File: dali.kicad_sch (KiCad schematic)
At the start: 15 parts, among them J2 DALI BUS, J3 DALI BUS, J4 DALI BUS, Q2 MMBT2222A, U1 TCLT1000, U2 TCLT1000

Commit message: Fix ESP32-S3-DEVKITC-1 bottom right pins
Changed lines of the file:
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@@
 	)
 	(symbol
+		(lib_name "FODM217D_1")
 		(lib_id "Isolator:FODM217D")
 		(at 166.37 29.21 0)

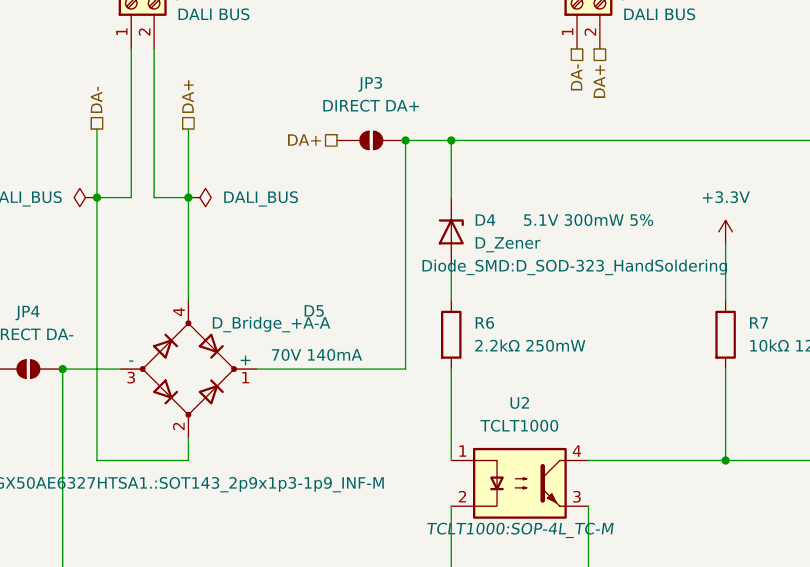
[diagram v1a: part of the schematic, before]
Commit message: Check and list components
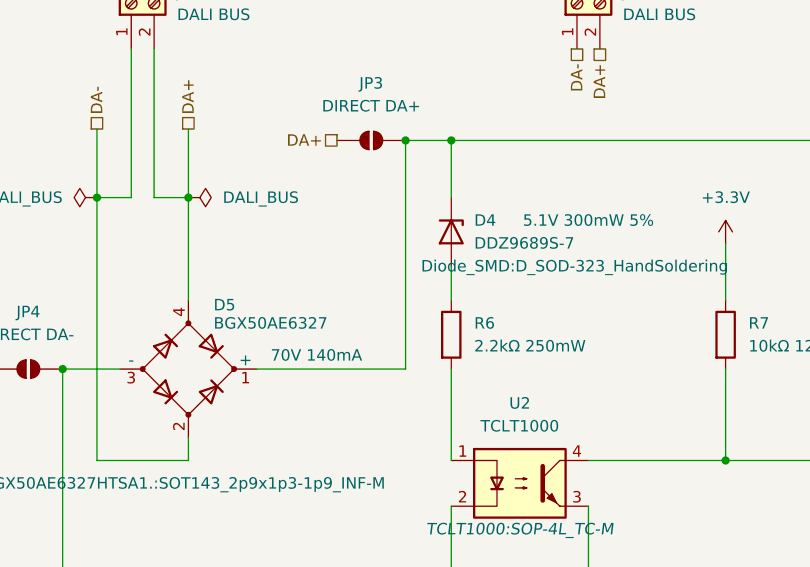
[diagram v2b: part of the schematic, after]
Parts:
- D4: value D_Zener -> DDZ9689S-7
- D5: value D_Bridge_+A-A -> BGX50AE6327
- Q2: footprint Package_TO_SOT_SMD:SOT-23 -> Package_TO_SOT_SMD:SOT-23_Handsoldering
- R6: footprint Resistor_SMD:R_0805_2012Metric_Pad1.20x1.40mm_HandSolder -> Resistor_SMD:R_1206_3216Metric_Pad1.30x1.75mm_HandSolder
- R8: footprint Resistor_SMD:R_0805_2012Metric_Pad1.20x1.40mm_HandSolder -> Resistor_SMD:R_2512_6332Metric_Pad1.40x3.35mm_HandSolder
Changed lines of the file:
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@@
 			)
 		)
-		(property "Footprint" "Resistor_SMD:R_0805_2012Metric_Pad1.20x1.40mm_HandSolder"
+		(property "Footprint" "Resistor_SMD:R_2512_6332Metric_Pad1.40x3.35mm_HandSolder"
 			(at 156.972 49.53 90)
 			(effects
@@
 		(dnp no)
 		(property "Reference" "D5"
-			(at 43.18 45.6498 0)
-			(effects
-				(font
-					(size 1.27 1.27)
-				)
-			)
-		)
-		(property "Value" "D_Bridge_+A-A"
-			(at 31.75 46.99 0)
+			(at 32.004 44.958 0)
+			(effects
+				(font
+					(size 1.27 1.27)
+				)
+				(justify left)
+			)
+		)
+		(property "Value" "BGX50AE6327"
+			(at 32.004 46.99 0)
 			(effects
 				(font
@@
 			)
 		)
-		(property "Datasheet" "~"
+		(property "Datasheet" "https://www.infineon.com/dgdl/bgx50aseries.pdf?folderId=db3a30431400ef6801141cc1c4cd04e8&fileId=db3a30431400ef6801141cc423c404e9"
 			(at 29.21 52.07 0)
 			(effects
@@
 			)
 		)
-		(property "Footprint" "Resistor_SMD:R_0805_2012Metric_Pad1.20x1.40mm_HandSolder"
+		(property "Footprint" "Resistor_SMD:R_1206_3216Metric_Pad1.30x1.75mm_HandSolder"
 			(at 56.642 48.26 90)
 			(effects
@@
 			)
 		)
-		(property "Footprint" "Package_TO_SOT_SMD:SOT-23"
+		(property "Footprint" "Package_TO_SOT_SMD:SOT-23_Handsoldering"
 			(at 118.11 43.815 0)
 			(effects
@@
 			)
 		)
-		(property "Datasheet" "https://assets.nexperia.com/documents/data-sheet/MMBT2222A.pdf"
+		(property "Datasheet" "https://www.onsemi.com/pdf/datasheet/mmbt2222lt1-d.pdf"
 			(at 123.19 41.91 0)
 			(effects
@@
 			)
 		)
-		(property "Value" "D_Zener"
+		(property "Value" "DDZ9689S-7"
 			(at 60.96 38.0999 90)
 			(effects
@@
 			)
 		)
-		(property "Datasheet" "~"
+		(property "Datasheet" "https://www.diodes.com/assets/Datasheets/ds30409.pdf"
 			(at 58.42 36.83 0)
 			(effects

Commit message: Remove the kitchen sink
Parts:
- removed J4: DALI BUS, TerminalBlock:TerminalBlock_bornier-2_P5.08mm, symbol Connector:Screw_Terminal_01x02
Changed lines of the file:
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@@
-		)
-	)
-	(hierarchical_label "DA-"
-		(shape passive)
-		(at 106.68 16.51 270)
-		(effects
-			(font
-				(size 1.27 1.27)
-			)
-			(justify right)
 		)
 	)
@@
 	(hierarchical_label "DA+"
 		(shape passive)
-		(at 109.22 16.51 270)
-		(effects
-			(font
-				(size 1.27 1.27)
-			)
-			(justify right)
-		)
-	)
-	(hierarchical_label "DA+"
-		(shape passive)
 		(at 29.21 25.4 90)
 		(effects
@@
 					(unit 1)
 				)
-			)
-		)
-	)
-	(symbol
-		(lib_id "Connector:Screw_Terminal_01x02")
-		(at 106.68 11.43 90)
-		(unit 1)
-		(exclude_from_sim no)
-		(in_bom yes)
-		(on_board yes)
-		(dnp no)
-		(fields_autoplaced yes)
-		(property "Reference" "J4"
-			(at 111.76 10.1599 90)
-			(effects
-				(font
-					(size 1.27 1.27)
-				)
-				(justify right)
-			)
-		)
-		(property "Value" "DALI BUS"
-			(at 111.76 12.6999 90)
-			(effects
-				(font
-					(size 1.27 1.27)
-				)
-				(justify right)
-			)
-		)
-		(property "Footprint" "TerminalBlock:TerminalBlock_bornier-2_P5.08mm"
-			(at 106.68 11.43 0)
-			(effects
-				(font
-					(size 1.27 1.27)
-				)
-				(hide yes)
-			)
-		)
-		(property "Datasheet" "~"
-			(at 106.68 11.43 0)
-			(effects
-				(font
-					(size 1.27 1.27)
-				)
-				(hide yes)
-			)
-		)
-		(property "Description" "Generic screw terminal, single row, 01x02, script generated (kicad-library-utils/schlib/autogen/connector/)"
-			(at 106.68 11.43 0)
-			(effects
-				(font
-					(size 1.27 1.27)
-				)
-				(hide yes)
-			)
-		)
-		(pin "1"
-		)
-		(pin "2"
-		)
-		(instances
-			(project "dali-pcb"
-				(path "/aa7f7e07-1f39-4222-a272-c9975d033b6d/da3e6e2b-6a82-47d9-9b10-47b7831d6589"
-					(reference "J4")
-					(unit 1)
-				)
